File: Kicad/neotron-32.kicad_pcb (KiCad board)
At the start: 4 copper layers, 166.9 x 140.7 mm, 97 parts, among them J1001 Conn_02x05, J101 Conn_02x06, J102 Conn_02x06, J103 Conn_02x04, J201 DIN-5 180 degree, J202 DIN-5 180 degree, J301 3.5mm Audio Jack TRS, J302 Conn_01x03_Male, J401 USB_B, J501 micro SD Card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

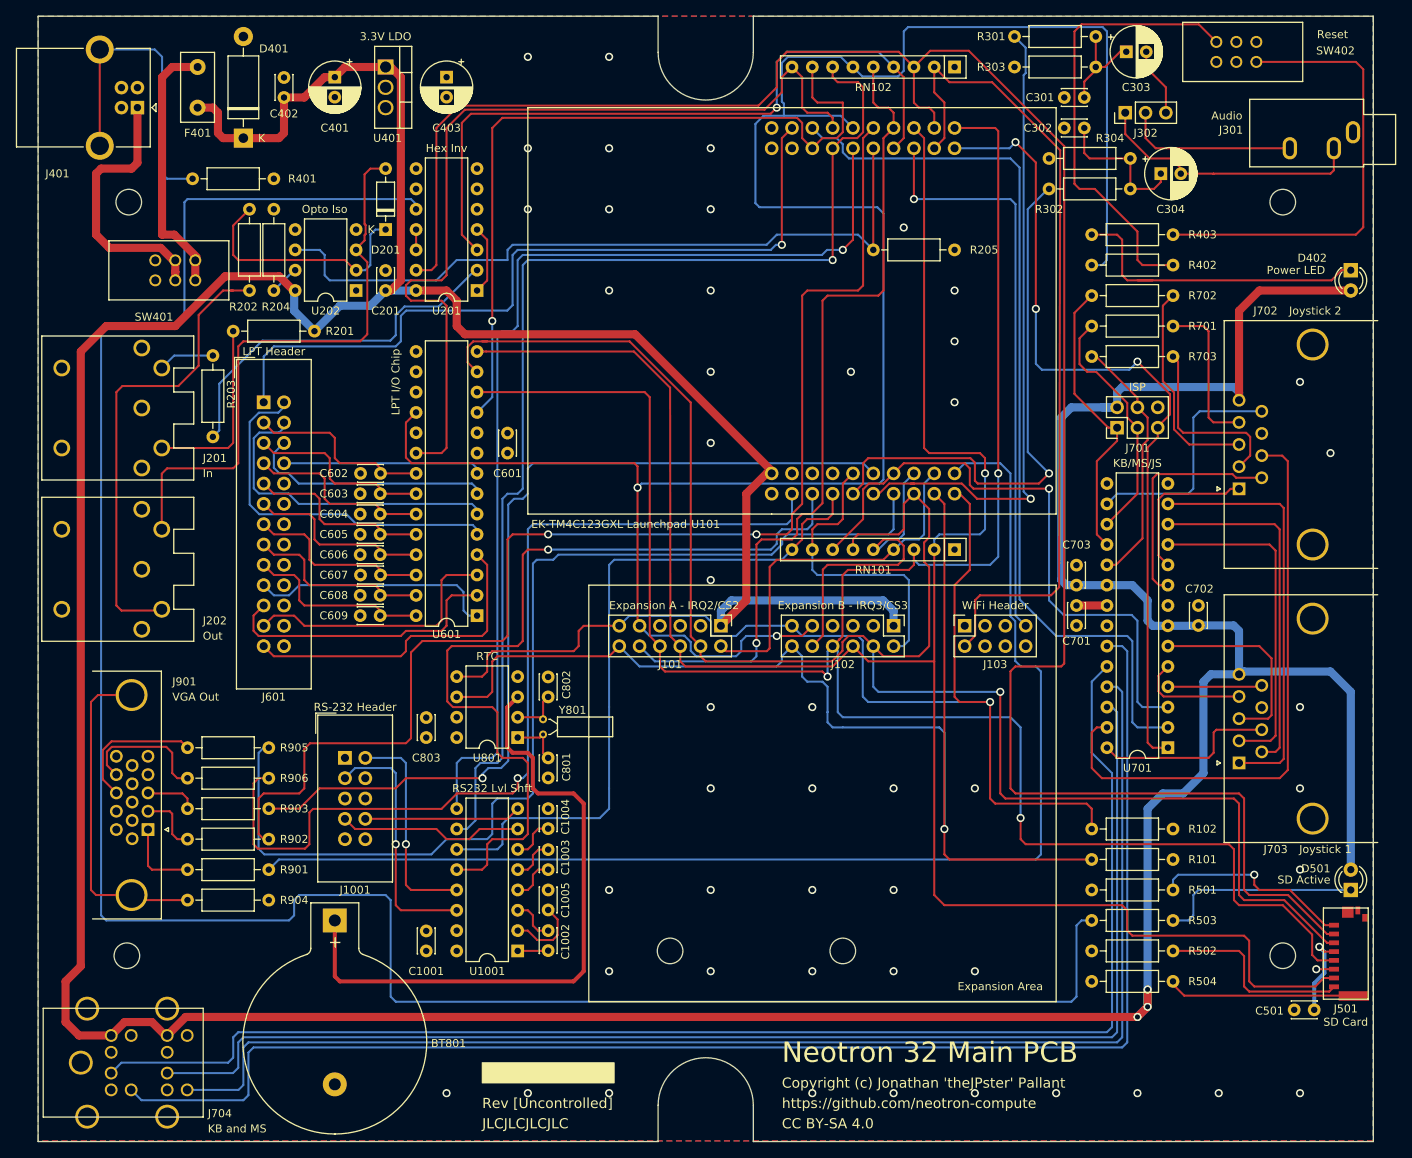
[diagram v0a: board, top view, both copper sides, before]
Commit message: Fixed up path to 3D models.
Also tidied up a few tracks to get better top pour.
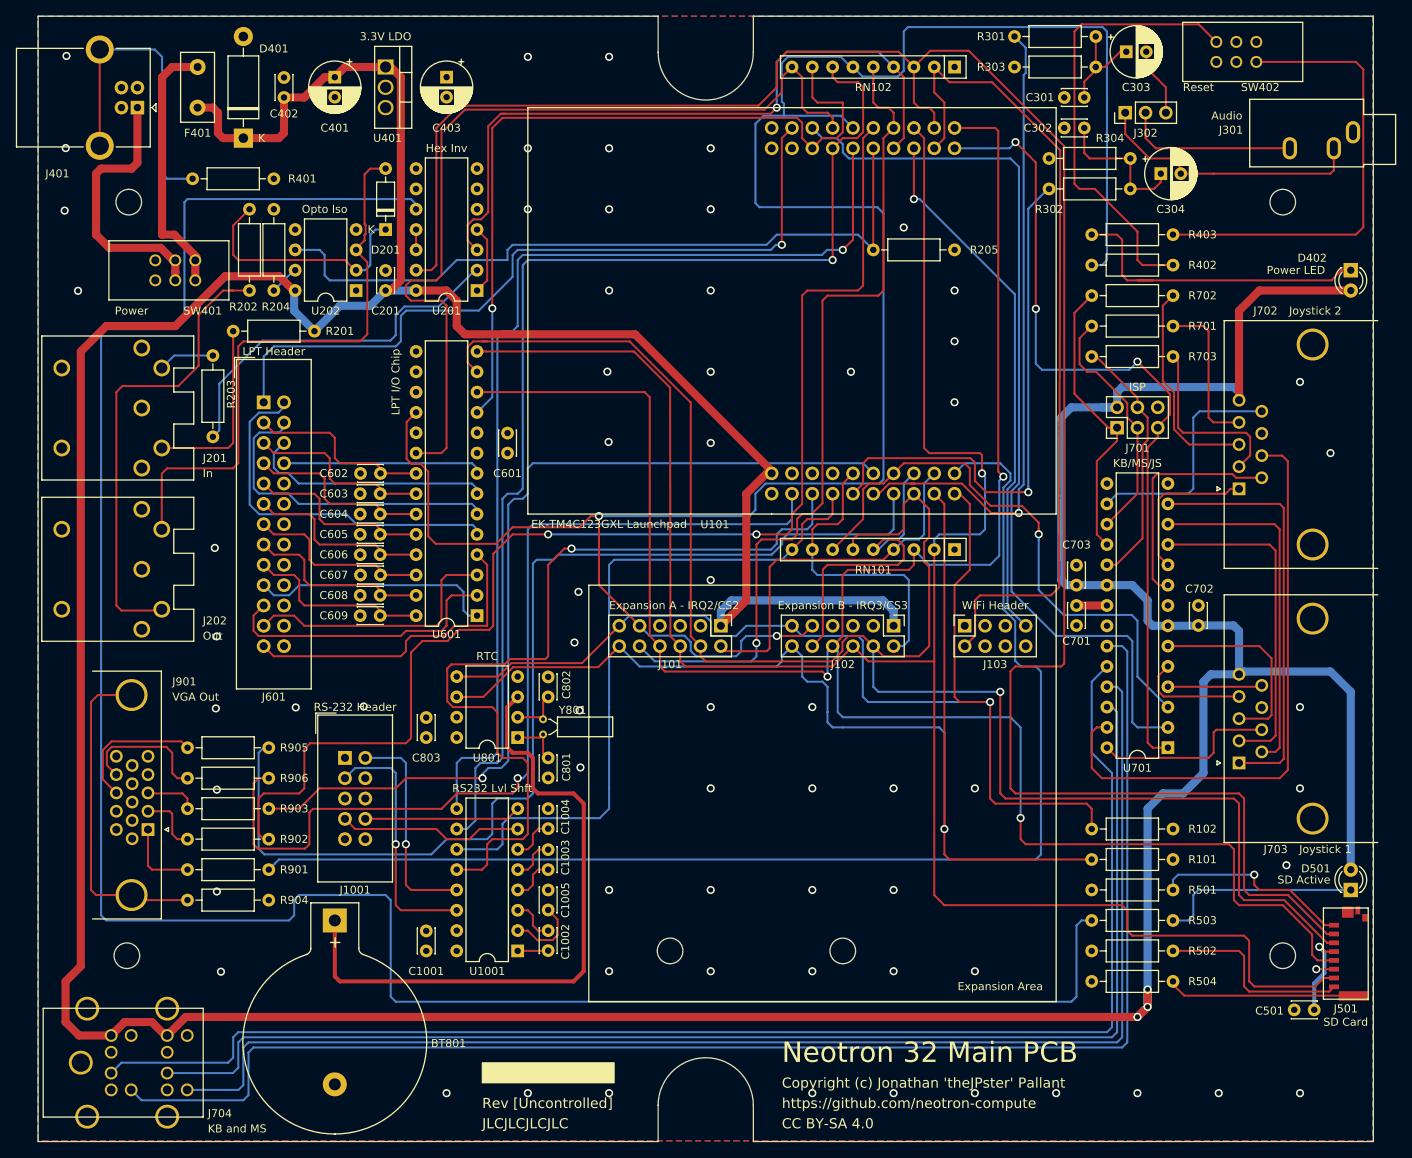
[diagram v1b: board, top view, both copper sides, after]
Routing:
- net /~RESET: track 270.9 -> 279.3 mm
- net /PD6_U2RX: track 72.5 -> 66.7 mm
- net /PE1_U7TX: track 76.5 -> 71.4 mm
- net /PA7_I2C_SDA: track 142.5 -> 140.3 mm
- net /PA6_I2C_SCL: track 153.2 -> 151.0 mm
- net /~PB2_STROBE: track 96.9 -> 94.9 mm
- net /PC7_MIDI_OUT: track 89.7 -> 87.8 mm
- net /PB7_VGA_GREEN: track 160.9 -> 159.1 mm
- net /PE4_AUDIO_L: track 68.4 -> 66.9 mm
- net /PE5_AUDIO_R: track 80.3 -> 81.2 mm
- net /PB0_U1RX: track 106.7 -> 105.9 mm
- net /PE0_U7RX: track 113.7 -> 114.4 mm
- net /PF1_VGA_RED: track 155.7 -> 156.4 mm
- net /~PF0_IRQ1: track 111.4 -> 110.8 mm
- net GND: vias 49 -> 67
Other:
- board text added: "Power"
